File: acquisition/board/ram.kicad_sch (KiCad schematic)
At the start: 19 parts, among them U2 XC7A50T-1FTG256C, U8 S27KS0642

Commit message: More power supply work, added PLL loop filter, soft start, began assigning footprints
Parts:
- C83: footprint (none) -> azonenberg_pcb:EIA_0603_CAP_NOSILK
- C84, C85, C86: footprint (none) -> azonenberg_pcb:EIA_0402_CAP_NOSILK
- R13, R14, R15, R16, R17, R18, R19, R20, R21, R34, R35, R36, R37: footprint (none) -> azonenberg_pcb:EIA_0402_RES_NOSILK
- U2: footprint (none) -> azonenberg_pcb:BGA_256_17x17_FULLARRAY_1MM_0.4MM_FTG256
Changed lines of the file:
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@@
   (title_block
     (title "Digitizer board")
-    (date "2022-07-05")
+    (date "2022-07-08")
     (rev "0.1")
     (company "A. Zonenberg")
@@
     (property "Reference" "R15" (id 0) (at 104.14 54.61 90))
     (property "Value" "33" (id 1) (at 99.06 55.88 90))
-    (property "Footprint" "" (id 2) (at 99.06 57.658 90)
+    (property "Footprint" "azonenberg_pcb:EIA_0402_RES_NOSILK" (id 2) (at 99.06 57.658 90)
       (effects (font (size 1.27 1.27)) hide)
     )
@@
       (effects (font (size 1.27 1.27)) (justify left))
     )
-    (property "Footprint" "" (id 2) (at 38.862 111.76 90)
+    (property "Footprint" "azonenberg_pcb:EIA_0402_RES_NOSILK" (id 2) (at 38.862 111.76 90)
       (effects (font (size 1.27 1.27)) hide)
     )
@@
     (property "Reference" "R36" (id 0) (at 43.18 66.04 90))
     (property "Value" "10K" (id 1) (at 43.18 68.58 90))
-    (property "Footprint" "" (id 2) (at 43.18 70.358 90)
+    (property "Footprint" "azonenberg_pcb:EIA_0402_RES_NOSILK" (id 2) (at 43.18 70.358 90)
       (effects (font (size 1.27 1.27)) hide)
     )
@@
       (effects (font (size 1.524 1.524)) (justify left))
     )
-    (property "Footprint" "" (id 2) (at 227.33 151.13 0)
-      (effects (font (size 1.524 1.524)))
+    (property "Footprint" "azonenberg_pcb:BGA_256_17x17_FULLARRAY_1MM_0.4MM_FTG256" (id 2) (at 227.33 151.13 0)
+      (effects (font (size 1.524 1.524)) hide)
     )
     (property "Datasheet" "" (id 3) (at 227.33 151.13 0)
@@
     (property "Reference" "R18" (id 0) (at 104.14 62.23 90))
     (property "Value" "33" (id 1) (at 99.06 63.5 90))
-    (property "Footprint" "" (id 2) (at 99.06 65.278 90)
+    (property "Footprint" "azonenberg_pcb:EIA_0402_RES_NOSILK" (id 2) (at 99.06 65.278 90)
       (effects (font (size 1.27 1.27)) hide)
     )
@@
     (property "Reference" "R20" (id 0) (at 104.14 67.31 90))
     (property "Value" "33" (id 1) (at 99.06 68.58 90))
-    (property "Footprint" "" (id 2) (at 99.06 70.358 90)
+    (property "Footprint" "azonenberg_pcb:EIA_0402_RES_NOSILK" (id 2) (at 99.06 70.358 90)
       (effects (font (size 1.27 1.27)) hide)
     )
@@
     (property "Reference" "R37" (id 0) (at 43.18 73.66 90))
     (property "Value" "10K" (id 1) (at 43.18 71.12 90))
-    (property "Footprint" "" (id 2) (at 43.18 72.898 90)
+    (property "Footprint" "azonenberg_pcb:EIA_0402_RES_NOSILK" (id 2) (at 43.18 72.898 90)
       (effects (font (size 1.27 1.27)) hide)
     )
@@
       (effects (font (size 1.27 1.27)) (justify left))
     )
-    (property "Footprint" "" (id 2) (at 38.862 99.06 90)
+    (property "Footprint" "azonenberg_pcb:EIA_0402_RES_NOSILK" (id 2) (at 38.862 99.06 90)
       (effects (font (size 1.27 1.27)) hide)
     )
@@
       (effects (font (size 1.27 1.27)) (justify left))
     )
-    (property "Footprint" "" (id 2) (at 65.7352 97.79 0)
+    (property "Footprint" "azonenberg_pcb:EIA_0603_CAP_NOSILK" (id 2) (at 65.7352 97.79 0)
       (effects (font (size 1.27 1.27)) hide)
     )
@@
       (effects (font (size 1.27 1.27)) (justify left))
     )
-    (property "Footprint" "" (id 2) (at 92.4052 97.79 0)
+    (property "Footprint" "azonenberg_pcb:EIA_0402_CAP_NOSILK" (id 2) (at 92.4052 97.79 0)
       (effects (font (size 1.27 1.27)) hide)
     )
@@
       (effects (font (size 1.27 1.27)) (justify left))
     )
-    (property "Footprint" "" (id 2) (at 107.6452 97.79 0)
+    (property "Footprint" "azonenberg_pcb:EIA_0402_CAP_NOSILK" (id 2) (at 107.6452 97.79 0)
       (effects (font (size 1.27 1.27)) hide)
     )
@@
     (property "Reference" "R21" (id 0) (at 104.14 69.85 90))
     (property "Value" "33" (id 1) (at 99.06 71.12 90))
-    (property "Footprint" "" (id 2) (at 99.06 72.898 90)
+    (property "Footprint" "azonenberg_pcb:EIA_0402_RES_NOSILK" (id 2) (at 99.06 72.898 90)
       (effects (font (size 1.27 1.27)) hide)
     )
@@
       (effects (font (size 1.27 1.27)) (justify left))
     )
-    (property "Footprint" "" (id 2) (at 78.4352 97.79 0)
+    (property "Footprint" "azonenberg_pcb:EIA_0402_CAP_NOSILK" (id 2) (at 78.4352 97.79 0)
       (effects (font (size 1.27 1.27)) hide)
     )
@@
     (property "Reference" "R17" (id 0) (at 104.14 59.69 90))
     (property "Value" "33" (id 1) (at 99.06 60.96 90))
-    (property "Footprint" "" (id 2) (at 99.06 62.738 90)
+    (property "Footprint" "azonenberg_pcb:EIA_0402_RES_NOSILK" (id 2) (at 99.06 62.738 90)
       (effects (font (size 1.27 1.27)) hide)
     )
@@
     (property "Reference" "R14" (id 0) (at 104.14 52.07 90))
     (property "Value" "33" (id 1) (at 99.06 53.34 90))
-    (property "Footprint" "" (id 2) (at 99.06 55.118 90)
+    (property "Footprint" "azonenberg_pcb:EIA_0402_RES_NOSILK" (id 2) (at 99.06 55.118 90)
       (effects (font (size 1.27 1.27)) hide)
     )
@@
     (property "Reference" "R16" (id 0) (at 104.14 57.15 90))
     (property "Value" "33" (id 1) (at 99.06 58.42 90))
-    (property "Footprint" "" (id 2) (at 99.06 60.198 90)
+    (property "Footprint" "azonenberg_pcb:EIA_0402_RES_NOSILK" (id 2) (at 99.06 60.198 90)
       (effects (font (size 1.27 1.27)) hide)
     )
@@
     (property "Reference" "R13" (id 0) (at 104.14 46.99 90))
     (property "Value" "33" (id 1) (at 99.06 48.26 90))
-    (property "Footprint" "" (id 2) (at 99.06 50.038 90)
+    (property "Footprint" "azonenberg_pcb:EIA_0402_RES_NOSILK" (id 2) (at 99.06 50.038 90)
       (effects (font (size 1.27 1.27)) hide)
     )
@@
     (property "Reference" "R19" (id 0) (at 104.14 64.77 90))
     (property "Value" "33" (id 1) (at 99.06 66.04 90))
-    (property "Footprint" "" (id 2) (at 99.06 67.818 90)
-      (effects (font (size 1.27 1.27)) hide)
-    )
+    (property "Footprint" "azonenberg_pcb:EIA_0402_RES_NOSILK" (id 2) (at 99.06 67.818 90)
+      (effects (font (size 1.27 1.27)) hide)
+    )

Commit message: Completed schematic after design review, ready for layout
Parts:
- R34, R35: value DNP -> 100
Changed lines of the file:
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@@
   (title_block
     (title "Digitizer board")
-    (date "2022-07-08")
+    (date "2022-07-17")
     (rev "0.1")
     (company "A. Zonenberg")
@@
       (effects (font (size 1.27 1.27)) (justify left))
     )
-    (property "Value" "DNP" (id 1) (at 42.418 113.6266 0)
+    (property "Value" "100" (id 1) (at 42.418 113.6266 0)
       (effects (font (size 1.27 1.27)) (justify left))
     )
@@
       (effects (font (size 1.27 1.27)) (justify left))
     )
-    (property "Value" "DNP" (id 1) (at 42.418 100.9266 0)
+    (property "Value" "100" (id 1) (at 42.418 100.9266 0)
       (effects (font (size 1.27 1.27)) (justify left))
     )

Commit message: Finished footprint assignment
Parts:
- U8: footprint (none) -> azonenberg_pcb:BGA_24_6x8_DEPOP1_1MM
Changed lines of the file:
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@@
   (title_block
     (title "Digitizer board")
-    (date "2022-07-17")
+    (date "2023-01-29")
     (rev "0.1")
     (company "A. Zonenberg")
@@
       (effects (font (size 1.524 1.524)))
     )
-    (property "Footprint" "" (id 2) (at 64.77 87.63 0)
+    (property "Footprint" "azonenberg_pcb:BGA_24_6x8_DEPOP1_1MM" (id 2) (at 64.77 87.63 0)
       (effects (font (size 1.524 1.524)) hide)
     )

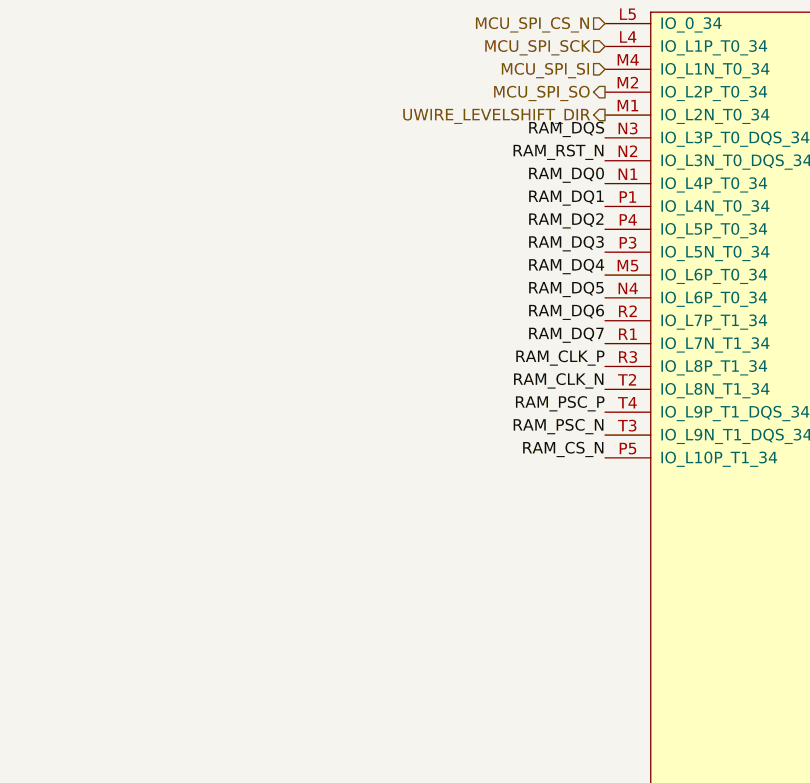
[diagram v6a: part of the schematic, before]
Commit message: Finished initial routing of RAM, hooked up almost all of first ADC
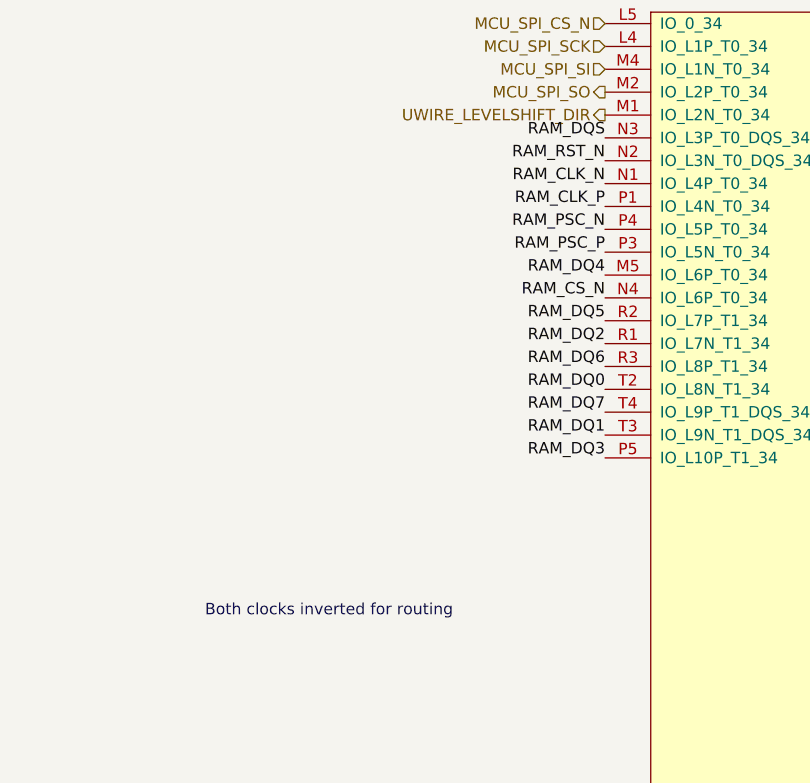
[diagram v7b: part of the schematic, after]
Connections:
- net RAM_CLK_N: now also U2.N1 (IO_L4P_T0_34); no longer U2.T2 (IO_L8N_T1_34)
- net RAM_CLK_P: now also U2.P1 (IO_L4N_T0_34); no longer U2.R3 (IO_L8P_T1_34)
- net RAM_CS_N: now also U2.N4 (IO_L6P_T0_34); no longer U2.P5 (IO_L10P_T1_34)
- net RAM_DQ0: now also U2.T2 (IO_L8N_T1_34); no longer U2.N1 (IO_L4P_T0_34)
- net RAM_DQ1: now also U2.T3 (IO_L9N_T1_DQS_34); no longer U2.P1 (IO_L4N_T0_34)
- net RAM_DQ2: now also U2.R1 (IO_L7N_T1_34); no longer U2.P4 (IO_L5P_T0_34)
- net RAM_DQ3: now also U2.P5 (IO_L10P_T1_34); no longer U2.P3 (IO_L5N_T0_34)
- net RAM_DQ5: now also U2.R2 (IO_L7P_T1_34); no longer U2.N4 (IO_L6P_T0_34)
- net RAM_DQ6: now also U2.R3 (IO_L8P_T1_34); no longer U2.R2 (IO_L7P_T1_34)
- net RAM_DQ7: now also U2.T4 (IO_L9P_T1_DQS_34); no longer U2.R1 (IO_L7N_T1_34)
- net RAM_PSC_N: now also U2.P4 (IO_L5P_T0_34); no longer U2.T3 (IO_L9N_T1_DQS_34)
- net RAM_PSC_P: now also U2.P3 (IO_L5N_T0_34); no longer U2.T4 (IO_L9P_T1_DQS_34)
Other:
- note added: "Both clocks inverted for routing"
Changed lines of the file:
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@@
+    (effects (font (size 1.27 1.27)) (justify left bottom))
+  )
+  (text "Both clocks inverted for routing" (at 177.8 92.71 0)
     (effects (font (size 1.27 1.27)) (justify left bottom))
   )
@@
     (effects (font (size 1.27 1.27)) (justify left bottom))
   )
-  (label "RAM_CLK_N" (at 222.25 67.31 180)
+  (label "RAM_CLK_N" (at 222.25 44.45 180)
     (effects (font (size 1.27 1.27)) (justify right bottom))
   )
@@
     (effects (font (size 1.27 1.27)) (justify left bottom))
   )
-  (label "RAM_DQ0" (at 222.25 44.45 180)
+  (label "RAM_DQ0" (at 222.25 67.31 180)
     (effects (font (size 1.27 1.27)) (justify right bottom))
   )
@@
     (effects (font (size 1.27 1.27)) (justify left bottom))
   )
-  (label "RAM_DQ6" (at 222.25 59.69 180)
+  (label "RAM_DQ6" (at 222.25 64.77 180)
     (effects (font (size 1.27 1.27)) (justify right bottom))
   )
@@
     (effects (font (size 1.27 1.27)) (justify left bottom))
   )
-  (label "RAM_PSC_P" (at 222.25 69.85 180)
+  (label "RAM_PSC_P" (at 222.25 52.07 180)
     (effects (font (size 1.27 1.27)) (justify right bottom))
   )
-  (label "RAM_DQ2" (at 222.25 49.53 180)
+  (label "RAM_DQ2" (at 222.25 62.23 180)
     (effects (font (size 1.27 1.27)) (justify right bottom))
   )
@@
     (effects (font (size 1.27 1.27)) (justify left bottom))
   )
-  (label "RAM_CLK_P" (at 222.25 64.77 180)
+  (label "RAM_CLK_P" (at 222.25 46.99 180)
     (effects (font (size 1.27 1.27)) (justify right bottom))
   )
@@
     (effects (font (size 1.27 1.27)) (justify right bottom))
   )
-  (label "RAM_DQ7" (at 222.25 62.23 180)
+  (label "RAM_DQ7" (at 222.25 69.85 180)
     (effects (font (size 1.27 1.27)) (justify right bottom))
   )
-  (label "RAM_DQ5" (at 222.25 57.15 180)
+  (label "RAM_DQ5" (at 222.25 59.69 180)
     (effects (font (size 1.27 1.27)) (justify right bottom))
   )
@@
     (effects (font (size 1.27 1.27)) (justify left bottom))
   )
-  (label "RAM_PSC_N" (at 222.25 72.39 180)
+  (label "RAM_PSC_N" (at 222.25 49.53 180)
     (effects (font (size 1.27 1.27)) (justify right bottom))
   )
-  (label "RAM_DQ1" (at 222.25 46.99 180)
+  (label "RAM_DQ1" (at 222.25 72.39 180)
     (effects (font (size 1.27 1.27)) (justify right bottom))
   )
@@
     (effects (font (size 1.27 1.27)) (justify right bottom))
   )
-  (label "RAM_DQ3" (at 222.25 52.07 180)
+  (label "RAM_DQ3" (at 222.25 74.93 180)
     (effects (font (size 1.27 1.27)) (justify right bottom))
   )
@@
     (effects (font (size 1.27 1.27)) (justify right bottom))
   )
-  (label "RAM_CS_N" (at 222.25 74.93 180)
+  (label "RAM_CS_N" (at 222.25 57.15 180)
     (effects (font (size 1.27 1.27)) (justify right bottom))
   )
